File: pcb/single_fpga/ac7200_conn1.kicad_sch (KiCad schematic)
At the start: 1 part, among them U97 ALINX AC7200 (XC7A200T-2FBG48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

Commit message: Changed position.
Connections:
- net +5V: now also U97.CON1_1 (VCCIN), U97.CON1_2 (VCCIN), U97.CON1_3 (VCCIN), U97.CON1_4 (VCCIN), U97.CON1_5 (VCCIN), U97.CON1_6 (VCCIN), U97.CON1_7 (VCCIN), U97.CON1_8 (VCCIN)
- net GND: now also U97.CON1_10 (GND), U97.CON1_19 (GND), U97.CON1_20 (GND), U97.CON1_29 (GND), U97.CON1_30 (GND), U97.CON1_39 (GND), U97.CON1_40 (GND), U97.CON1_49 (GND), U97.CON1_50 (GND), U97.CON1_59 (GND), U97.CON1_60 (GND), U97.CON1_69 (GND), U97.CON1_70 (GND), U97.CON1_9 (GND)
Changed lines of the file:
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@@
-	(wire
-		(pts
-			(xy 135.89 72.39) (xy 140.97 72.39)
-		)
-		(stroke
-			(width 0)
-			(type default)
-		)
-	)
 	(wire
 		(pts
@@
 	(wire
 		(pts
+			(xy 135.41 72.39) (xy 140.97 72.39)
+		)
+		(stroke
+			(width 0)
+			(type default)
+		)
+	)
+	(wire
+		(pts
 			(xy 140.97 100.33) (xy 140.97 104.14)
 		)
@@
 	(wire
 		(pts
-			(xy 135.89 97.79) (xy 140.97 97.79)
-		)
-		(stroke
-			(width 0)
-			(type default)
-		)
-	)
-	(wire
-		(pts
 			(xy 90.17 57.15) (xy 90.17 59.69)
 		)
@@
 	(wire
 		(pts
+			(xy 135.41 125.73) (xy 140.97 125.73)
+		)
+		(stroke
+			(width 0)
+			(type default)
+		)
+	)
+	(wire
+		(pts
 			(xy 140.97 97.79) (xy 140.97 100.33)
 		)
@@
 	(wire
 		(pts
+			(xy 135.41 100.33) (xy 140.97 100.33)
+		)
+		(stroke
+			(width 0)
+			(type default)
+		)
+	)
+	(wire
+		(pts
+			(xy 135.41 74.93) (xy 140.97 74.93)
+		)
+		(stroke
+			(width 0)
+			(type default)
+		)
+	)
+	(wire
+		(pts
 			(xy 95.25 72.39) (xy 90.17 72.39)
 		)
@@
 	(wire
 		(pts
-			(xy 135.89 100.33) (xy 140.97 100.33)
-		)
-		(stroke
-			(width 0)
-			(type default)
-		)
-	)
-	(wire
-		(pts
 			(xy 90.17 72.39) (xy 90.17 74.93)
 		)
@@
 	(wire
 		(pts
-			(xy 135.89 125.73) (xy 140.97 125.73)
-		)
-		(stroke
-			(width 0)
-			(type default)
-		)
-	)
-	(wire
-		(pts
 			(xy 90.17 43.18) (xy 90.17 52.07)
 		)
@@
 	(wire
 		(pts
+			(xy 135.41 123.19) (xy 140.97 123.19)
+		)
+		(stroke
+			(width 0)
+			(type default)
+		)
+	)
+	(wire
+		(pts
 			(xy 90.17 148.59) (xy 90.17 151.13)
 		)
@@
 	(wire
 		(pts
-			(xy 135.89 123.19) (xy 140.97 123.19)
-		)
-		(stroke
-			(width 0)
-			(type default)
-		)
-	)
-	(wire
-		(pts
 			(xy 90.17 100.33) (xy 90.17 104.14)
 		)
@@
 	(wire
 		(pts
-			(xy 135.89 74.93) (xy 140.97 74.93)
-		)
-		(stroke
-			(width 0)
-			(type default)
-		)
-	)
-	(wire
-		(pts
 			(xy 90.17 97.79) (xy 90.17 100.33)
+		)
+		(stroke
+			(width 0)
+			(type default)
+		)
+	)
+	(wire
+		(pts
+			(xy 135.41 97.79) (xy 140.97 97.79)
 		)
 		(stroke
@@
 	(symbol
 		(lib_id "single_fpga:AC7200")
-		(at 115.57 101.6 0)
+		(at 115.33 101.6 0)
 		(unit 1)
 		(body_style 1)
@@
 		(fields_autoplaced yes)
 		(property "Reference" "U97"
-			(at 115.57 40.64 0)
+			(at 115.33 40.64 0)
 			(show_name no)
 			(do_not_autoplace no)
@@
 		)
 		(property "Value" "ALINX AC7200 (XC7A200T-2FBG484I)"
-			(at 115.57 43.18 0)
+			(at 115.33 43.18 0)
 			(show_name no)
 			(do_not_autoplace no)
@@
 		)
 		(property "Footprint" "single_fpga:AC7200"
-			(at 115.57 101.6 0)
+			(at 115.33 101.6 0)
 			(hide yes)
 			(show_name no)
@@
 		)
 		(property "Datasheet" "docs/AC7200_User_Manual.pdf"
-			(at 115.57 101.6 0)
+			(at 115.33 101.6 0)
 			(hide yes)
 			(show_name no)
@@
 		)
 		(property "Description" "ALINX AC7200 XC7A200T-2FBG484I Artix-7 FPGA SOM, 45x55mm, 4x 80-pin/0.5mm B2B connectors (Unit A=CON1 VCCIN/GND+BANK34+BANK13+XADC, Unit B=CON2 BANK13+BANK14, Unit C=CON3 BANK15+BANK16+JTAG (TCK/TDI/TDO/TMS on pins 77-80 -- a SEPARATE on-module 6-pin JTAG header J1 also exists, not modeled here), Unit D=CON4 BANK16+GTP transceivers). Every pin cross-checked against ALINX's own real user manual (docs/AC7200_User_Manual.pdf) -- CON2/CON3/CON4 and CON1 pins 1-72 matched an earlier web-transcription exactly; CON1 pins 73-80 (previously unverified placeholder) now filled in from the real manual. ONE correction applied: CON1 pin 27 is printed as 'B13_L7_P' in ALINX's own manual (same as pin 25) -- a real duplicate/typo in their document (different FPGA balls AB11 vs AB12, and every other one of the 320 pins alternates P/N without exception) -- corrected here to B13_L7_N. Module standalone-power (J3, 2-pin +5V/GND) and JTAG (J1, 6-pin) headers exist on the module but are not part of this symbol (carrier-board-facing CON1-4 only)."
-			(at 115.57 101.6 0)
+			(at 115.33 101.6 0)
 			(hide yes)
 			(show_name no)

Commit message: Fixed.
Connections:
- net +5V: no longer U97.CON1_1 (VCCIN), U97.CON1_2 (VCCIN), U97.CON1_3 (VCCIN), U97.CON1_4 (VCCIN), U97.CON1_5 (VCCIN), U97.CON1_6 (VCCIN), U97.CON1_7 (VCCIN), U97.CON1_8 (VCCIN)
- net GND: no longer U97.CON1_10 (GND), U97.CON1_19 (GND), U97.CON1_20 (GND), U97.CON1_29 (GND), U97.CON1_30 (GND), U97.CON1_39 (GND), U97.CON1_40 (GND), U97.CON1_49 (GND), U97.CON1_50 (GND), U97.CON1_59 (GND), U97.CON1_60 (GND), U97.CON1_69 (GND), U97.CON1_70 (GND), U97.CON1_9 (GND)
- no-connect marks 19 -> 13

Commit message: Reorganized sheets for two-boards. Fixed connector off-grid problems.
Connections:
- net +5V: now also U97.CON1_1 (VCCIN), U97.CON1_2 (VCCIN), U97.CON1_3 (VCCIN), U97.CON1_4 (VCCIN), U97.CON1_5 (VCCIN), U97.CON1_6 (VCCIN), U97.CON1_7 (VCCIN), U97.CON1_8 (VCCIN)
- net GND: now also U97.CON1_10 (GND), U97.CON1_19 (GND), U97.CON1_29 (GND), U97.CON1_30 (GND), U97.CON1_39 (GND), U97.CON1_40 (GND), U97.CON1_49 (GND), U97.CON1_50 (GND), U97.CON1_59 (GND), U97.CON1_60 (GND), U97.CON1_69 (GND), U97.CON1_70 (GND), U97.CON1_9 (GND)
- no-connect marks 13 -> 19

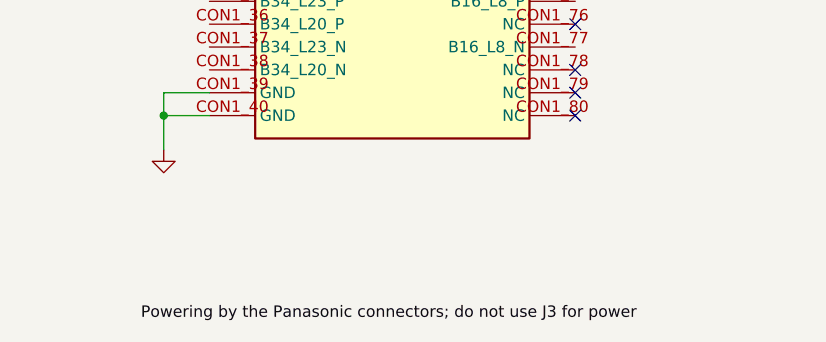
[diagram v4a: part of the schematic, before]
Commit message: Fixed another off-grid issue. Connected power and DATA_?? pins to inter-board connector.
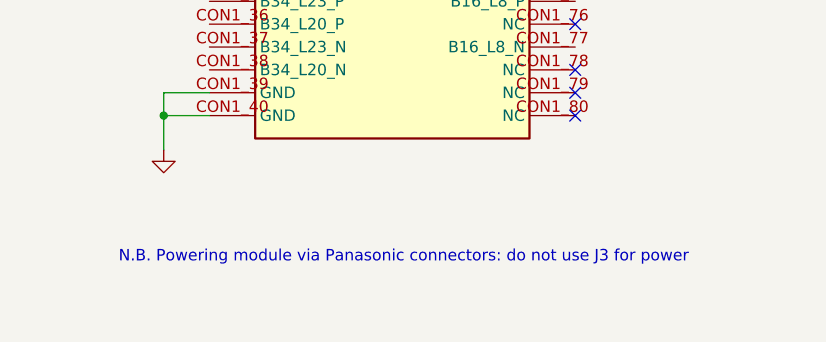
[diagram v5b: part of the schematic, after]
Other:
- note added: "N.B. Powering module via Panasonic connectors: do not use J3 for power"

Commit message: Updated all refdes's.
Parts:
- renumbered U97 to U109
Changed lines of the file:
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@@
 		(dnp no)
 		(fields_autoplaced yes)
-		(property "Reference" "U97"
+		(property "Reference" "U109"
 			(at 115.57 40.64 0)
 			(show_name no)
@@
 			(project "top"
 				(path "/12638caa-1907-413e-8e98-06abbbf6ccbc/8ee3463b-0816-4e24-be6c-9811f4c49ad3/99fd9359-fefb-4a8a-9183-e71ec276431f"
-					(reference "U97")
+					(reference "U109")
 					(unit 1)
 				)
@@
 		(dnp no)
 		(fields_autoplaced yes)
-		(property "Reference" "#PWR01"
+		(property "Reference" "#PWR0431"
 			(at 90.17 86.36 0)
 			(hide yes)
@@
 			(project "top"
 				(path "/12638caa-1907-413e-8e98-06abbbf6ccbc/8ee3463b-0816-4e24-be6c-9811f4c49ad3/99fd9359-fefb-4a8a-9183-e71ec276431f"
-					(reference "#PWR01")
+					(reference "#PWR0431")
 					(unit 1)
 				)
@@
 		(dnp no)
 		(fields_autoplaced yes)
-		(property "Reference" "#PWR02"
+		(property "Reference" "#PWR0430"
 			(at 90.17 45.72 0)
 			(hide yes)
@@
 			(project "top"
 				(path "/12638caa-1907-413e-8e98-06abbbf6ccbc/8ee3463b-0816-4e24-be6c-9811f4c49ad3/99fd9359-fefb-4a8a-9183-e71ec276431f"
-					(reference "#PWR02")
+					(reference "#PWR0430")
 					(unit 1)
 				)
@@
 		(dnp no)
 		(fields_autoplaced yes)
-		(property "Reference" "#PWR03"
+		(property "Reference" "#PWR0436"
 			(at 140.97 110.49 0)
 			(hide yes)
@@
 			(project "top"
 				(path "/12638caa-1907-413e-8e98-06abbbf6ccbc/8ee3463b-0816-4e24-be6c-9811f4c49ad3/99fd9359-fefb-4a8a-9183-e71ec276431f"
-					(reference "#PWR03")
+					(reference "#PWR0436")
 					(unit 1)
 				)
@@
 		(dnp no)
 		(fields_autoplaced yes)
-		(property "Reference" "#PWR04"
+		(property "Reference" "#PWR0435"
 			(at 140.97 85.09 0)
 			(hide yes)
@@
 			(project "top"
 				(path "/12638caa-1907-413e-8e98-06abbbf6ccbc/8ee3463b-0816-4e24-be6c-9811f4c49ad3/99fd9359-fefb-4a8a-9183-e71ec276431f"
-					(reference "#PWR04")
+					(reference "#PWR0435")
 					(unit 1)
 				)
@@
 		(dnp no)
 		(fields_autoplaced yes)
-		(property "Reference" "#PWR05"
+		(property "Reference" "#PWR0432"
 			(at 90.17 110.49 0)
 			(hide yes)
@@
 			(project "top"
 				(path "/12638caa-1907-413e-8e98-06abbbf6ccbc/8ee3463b-0816-4e24-be6c-9811f4c49ad3/99fd9359-fefb-4a8a-9183-e71ec276431f"
-					(reference "#PWR05")
+					(reference "#PWR0432")
 					(unit 1)
 				)
@@
 		(dnp no)
 		(fields_autoplaced yes)
-		(property "Reference" "#PWR06"
+		(property "Reference" "#PWR0434"
 			(at 90.17 161.29 0)
 			(hide yes)
@@
 			(project "top"
 				(path "/12638caa-1907-413e-8e98-06abbbf6ccbc/8ee3463b-0816-4e24-be6c-9811f4c49ad3/99fd9359-fefb-4a8a-9183-e71ec276431f"
-					(reference "#PWR06")
+					(reference "#PWR0434")
 					(unit 1)
 				)
@@
 		(dnp no)
 		(fields_autoplaced yes)
-		(property "Reference" "#PWR07"
+		(property "Reference" "#PWR0433"
 			(at 90.17 135.89 0)
 			(hide yes)
@@
 			(project "top"
 				(path "/12638caa-1907-413e-8e98-06abbbf6ccbc/8ee3463b-0816-4e24-be6c-9811f4c49ad3/99fd9359-fefb-4a8a-9183-e71ec276431f"
-					(reference "#PWR07")
+					(reference "#PWR0433")
 					(unit 1)
 				)
@@
 		(dnp no)
 		(fields_autoplaced yes)
-		(property "Reference" "#PWR08"
+		(property "Reference" "#PWR0437"
 			(at 140.97 135.89 0)
 			(hide yes)
@@
 			(project "top"
 				(path "/12638caa-1907-413e-8e98-06abbbf6ccbc/8ee3463b-0816-4e24-be6c-9811f4c49ad3/99fd9359-fefb-4a8a-9183-e71ec276431f"
-					(reference "#PWR08")
+					(reference "#PWR0437")
 					(unit 1)
 				)

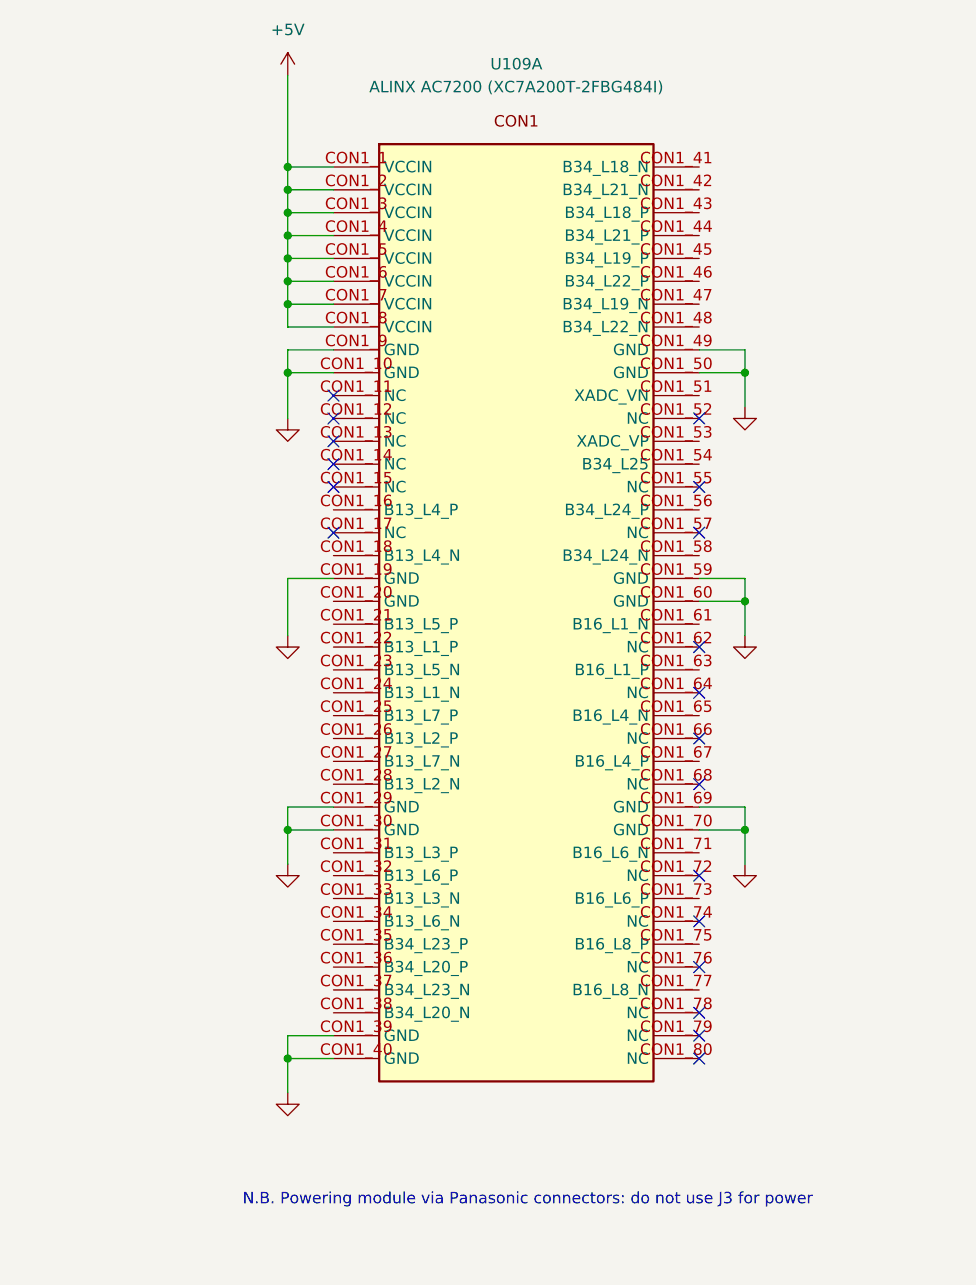
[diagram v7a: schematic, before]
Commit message: Added Ethernet interface. Fixed power rails. ERC-clean.
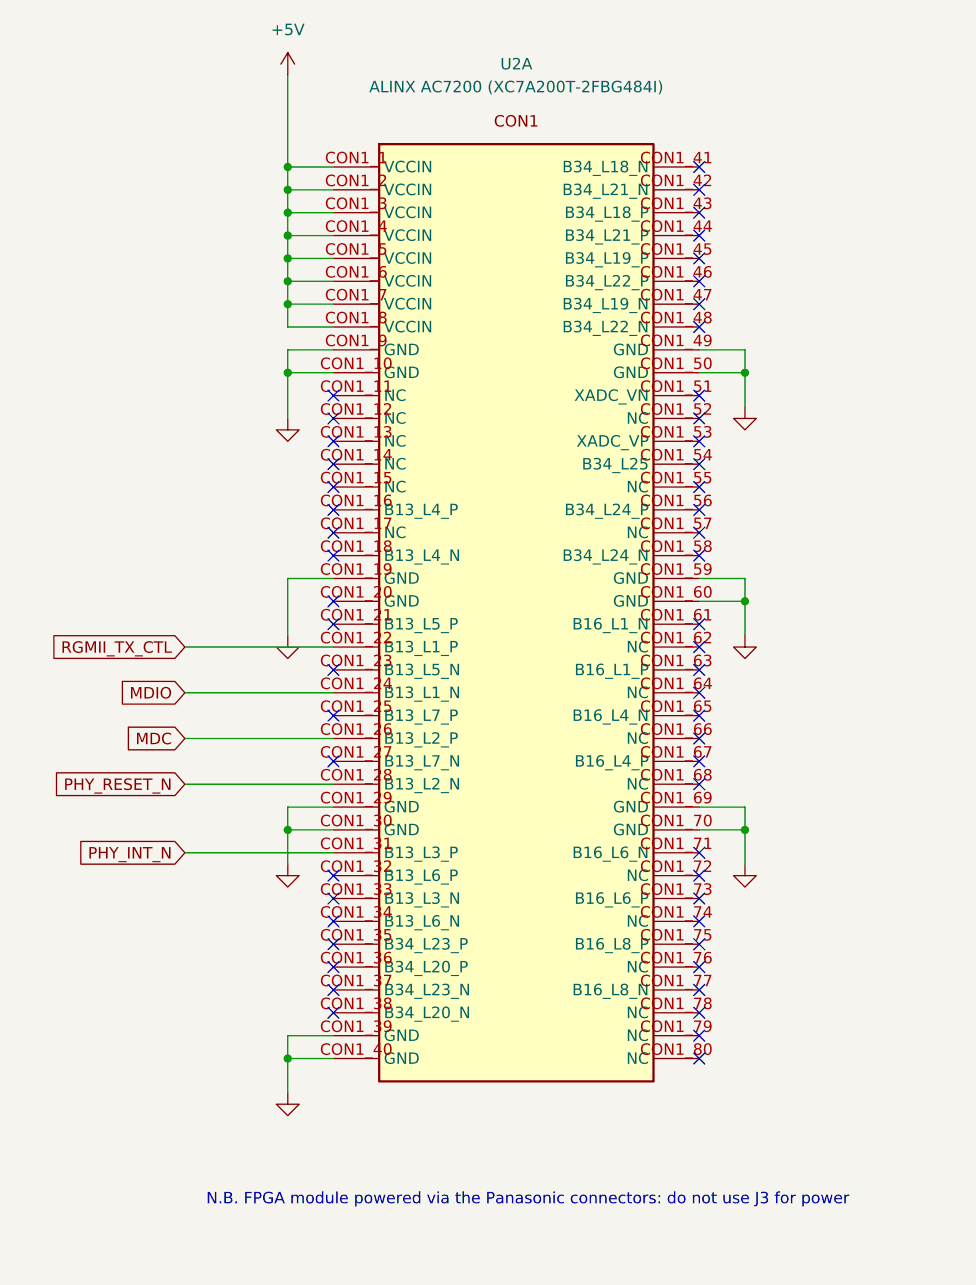
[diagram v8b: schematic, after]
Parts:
- renumbered U109 to U2
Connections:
- net RGMII_TX_CTL: now reaches U2.CON1_22 (B13_L1_P)
- net MDIO: now reaches U2.CON1_24 (B13_L1_N)
- net MDC: now reaches U2.CON1_26 (B13_L2_P)
- net PHY_RESET_N: now reaches U2.CON1_28 (B13_L2_N)
- net PHY_INT_N: now reaches U2.CON1_31 (B13_L3_P)
- no-connect marks 19 -> 54
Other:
- note added: "N.B. FPGA module powered via the Panasonic connectors: do not use J3 for power"
- note removed: "N.B. Powering module via Panasonic connectors: do not use J3 for power"
